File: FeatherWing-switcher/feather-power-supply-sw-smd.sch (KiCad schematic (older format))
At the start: 25 parts, among them J1 5.08mm, J2 Conn_01x12, J3 Conn_01x16, J4 QWIIC, U1 TPS5405DR

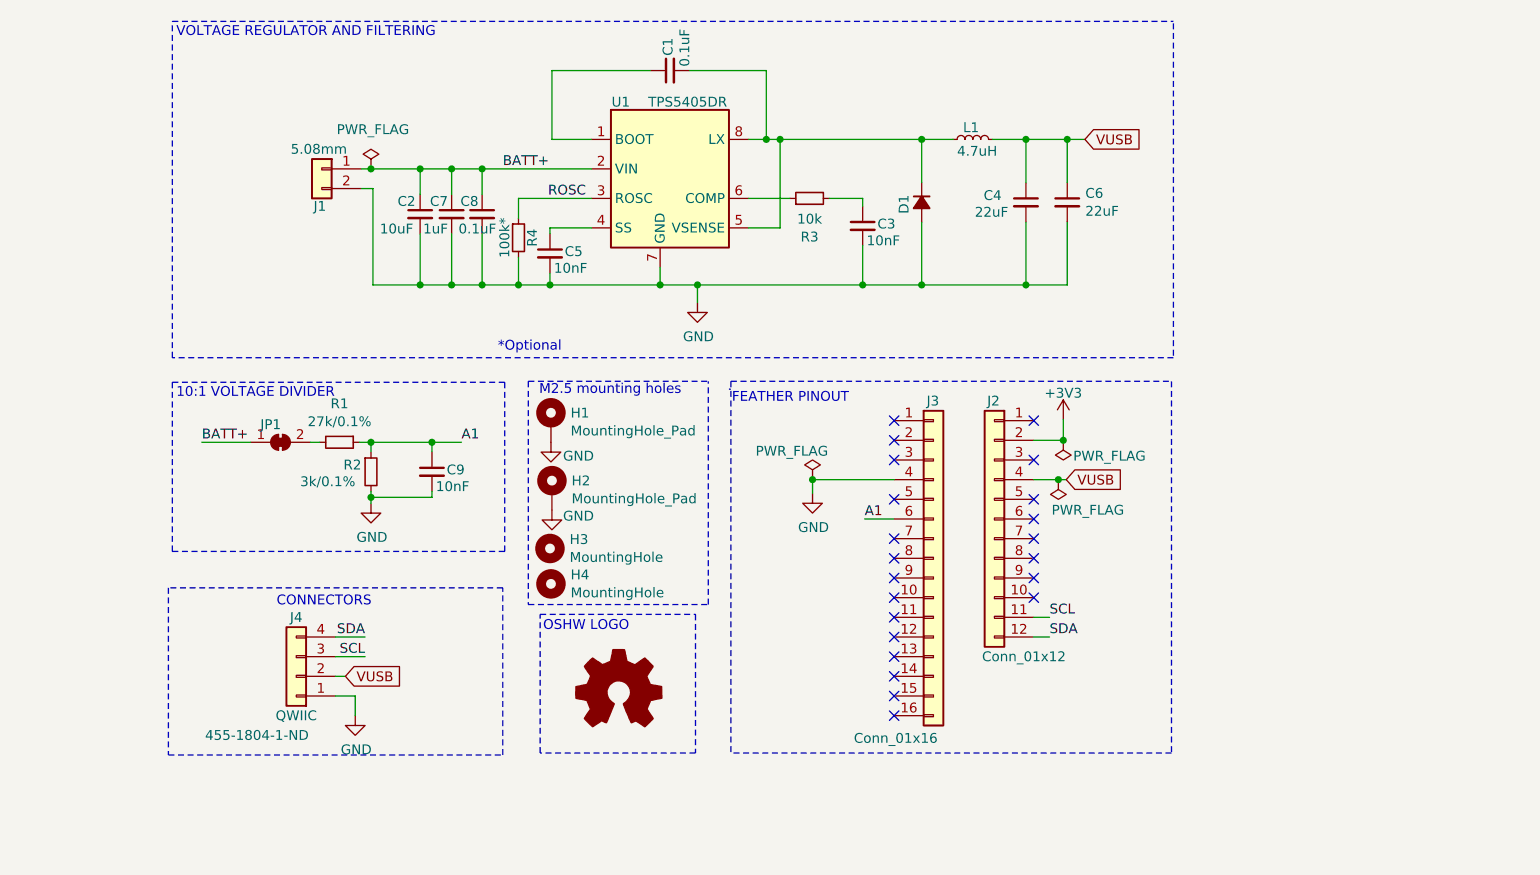
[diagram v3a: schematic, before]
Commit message: adds proto and leds
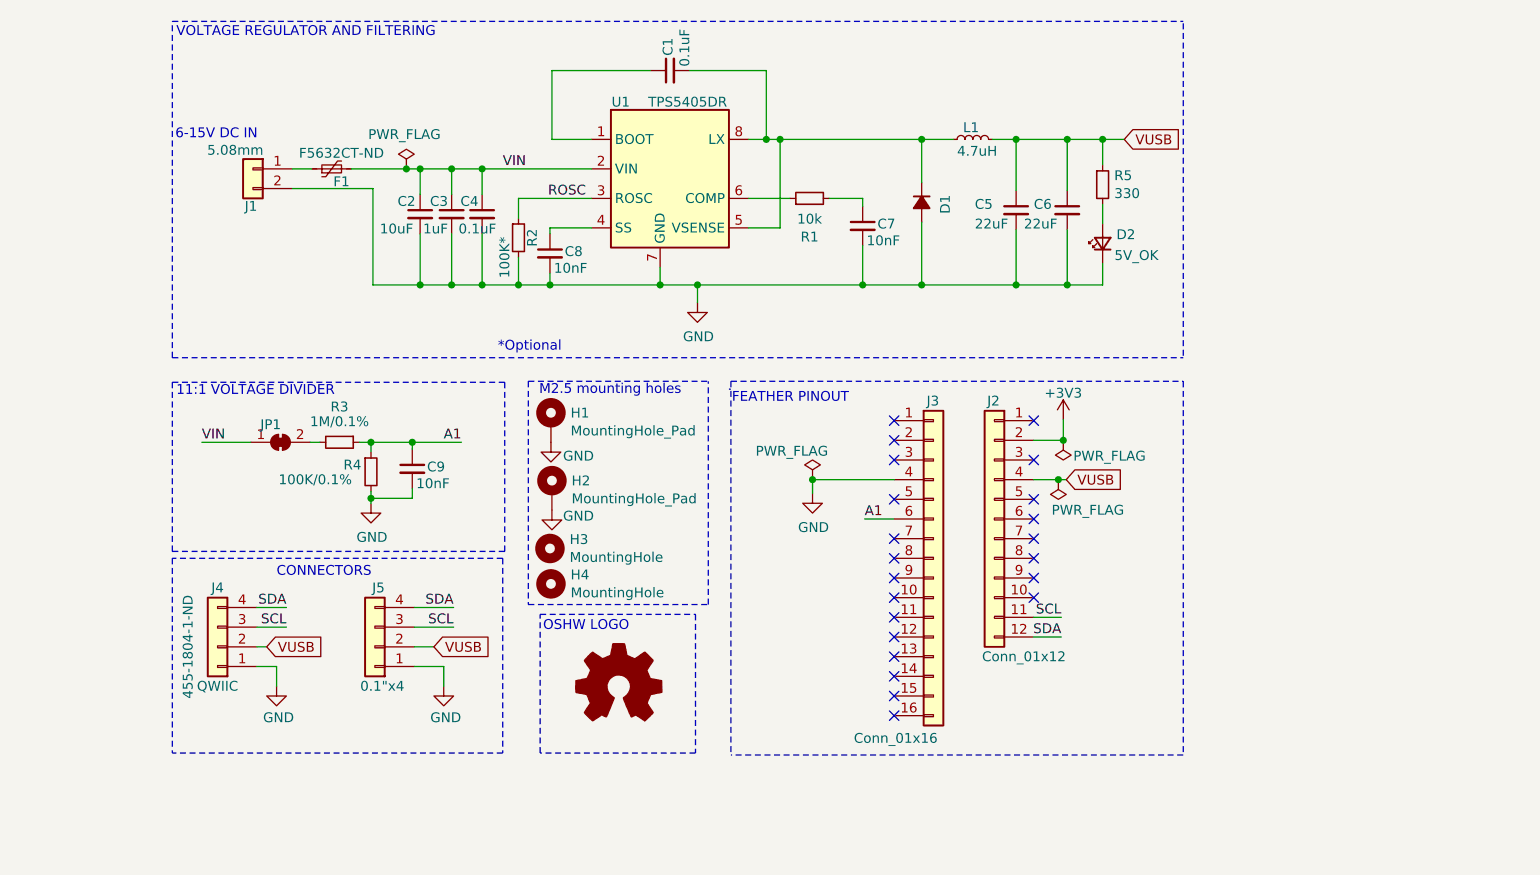
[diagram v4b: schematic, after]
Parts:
- added D2: 5V_OK, LED_SMD:LED_0805_2012Metric_Castellated, symbol Device:LED_Small
- added F1: 24V 1.1A, Fuse:Fuse_1812_4532Metric_Castellated, symbol Device:Polyfuse_Small
- added J5: 0.1\"x4, Connector_PinHeader_2.54mm:PinHeader_1x04_P2.54mm_Vertical, symbol Connector_Generic:Conn_01x04
- added LOGO1: Logo_Open_Hardware_Small, Symbol:OSHW-Symbol_6.7x6mm_SilkScreen, symbol Graphic:Logo_Open_Hardware_Small
- added R5: 330, Resistor_SMD:R_0603_1608Metric_Pad1.05x0.95mm_HandSolder, symbol Device:R_Small
- R2: renamed from R4; value 100k* -> 100K*
- R3: renamed from R1; value 27k/0.1% -> 1M/0.1%
- R4: renamed from R2; value 3k/0.1% -> 100K/0.1%
- renumbered C7 to C3, C8 to C4, C4 to C5, C3 to C7, C5 to C8, R3 to R1
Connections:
- net GND: now also D2.1 (K), J5.1 (Pin_1)
- net SCL: now also J5.3 (Pin_3)
- net SDA: now also J5.4 (Pin_4)
- net VUSB: now also J5.2 (Pin_2), R5.1
- net BATT+ renamed VIN
- net VIN: now also F1.2; no longer J1.1 (Pin_1)
- new net: F1.1, J1.1 (Pin_1)
- new net: D2.2 (A), R5.2
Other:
- note added: "11:1 VOLTAGE DIVIDER"
- note added: "6-15V DC IN"
- note removed: "10:1 VOLTAGE DIVIDER"
- moved on the sheet: C5, C6, C9, J1, J4

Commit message: major updates to route buses using  copper pours
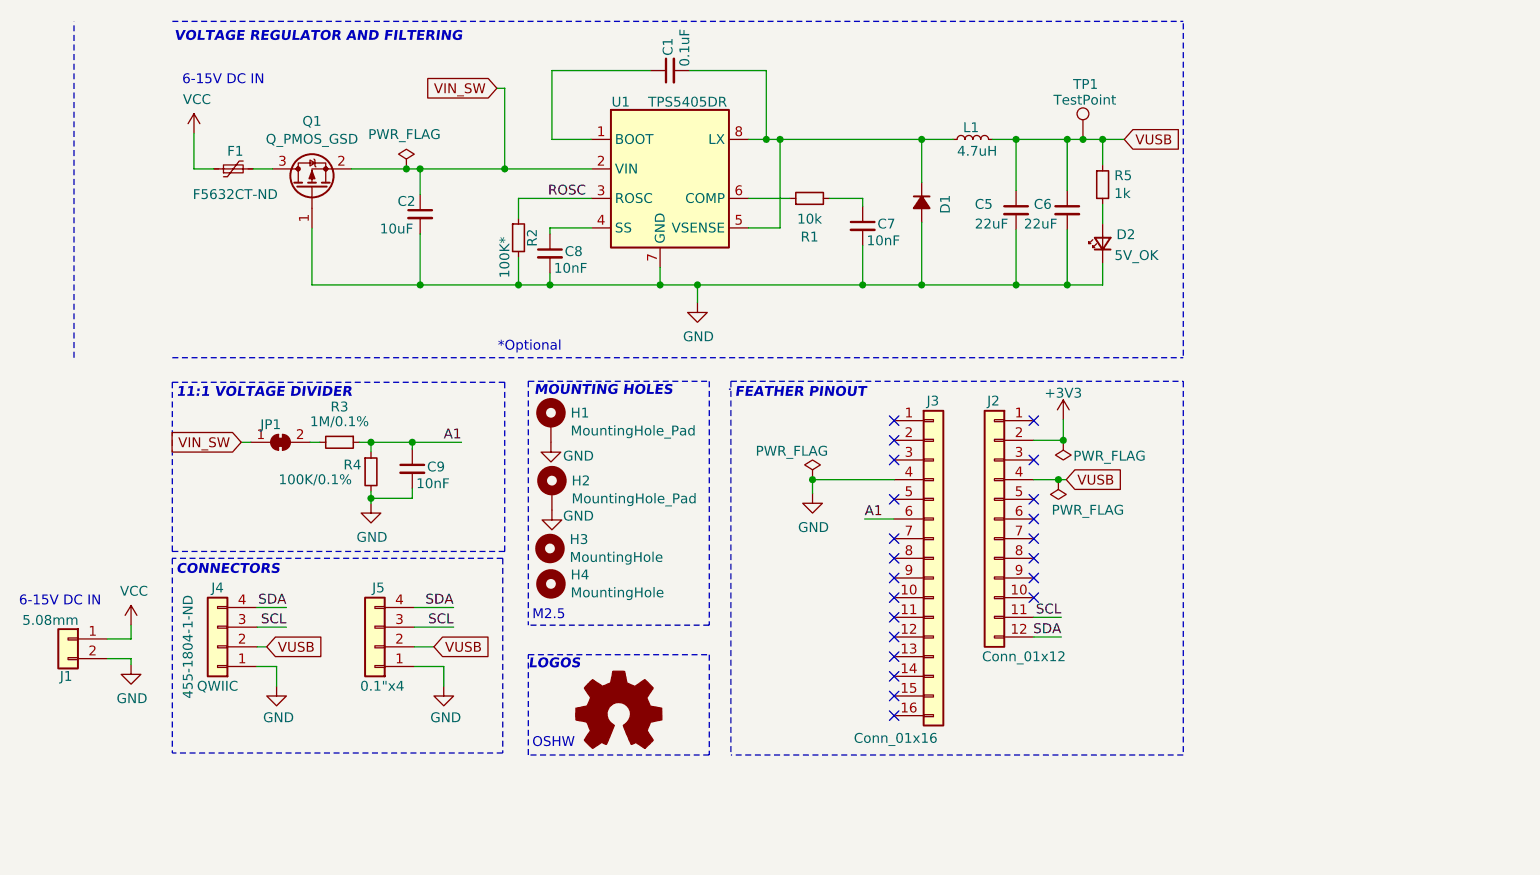
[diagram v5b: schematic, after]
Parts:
- removed C3: 1uF, Capacitor_SMD:C_0603_1608Metric_Pad1.05x0.95mm_HandSolder, symbol Device:C_Small
- removed C4: 0.1uF, Capacitor_SMD:C_0603_1608Metric_Pad1.05x0.95mm_HandSolder, symbol Device:C_Small
- added Q1: Q_PMOS_GSD, Package_TO_SOT_SMD:TSOT-23, symbol Device:Q_PMOS_GSD
- added TP1: TestPoint, TestPoint:TestPoint_Pad_D1.5mm, symbol Connector:TestPoint
- R5: value 330 -> 1k
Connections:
- net GND: now also Q1.1 (G)
- net VUSB: now also TP1.1
- net VCC: now reaches F1.1, J1.1 (Pin_1)
- net VIN renamed VIN_SW
- net VIN_SW: now also Q1.2 (S); no longer F1.2
- new net: F1.2, Q1.3 (D)
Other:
- note added: "LOGOS"
- note added: "M2.5"
- note added: "MOUNTING HOLES"
- note added: "OSHW"
- note removed: "M2.5 mounting holes"
- note removed: "OSHW LOGO"
- moved on the sheet: F1, J1
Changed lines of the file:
@@
-$EndComp
-$Comp
-L Connector_Generic:Conn_01x16 J3
-U 1 1 5F435436
-P 6940 4300
-F 0 "J3" H 6905 5100 50  0000 L CNN
-F 1 "Conn_01x16" H 6535 3385 50  0000 L CNN
-F 2 "Connector_PinHeader_2.54mm:PinHeader_1x16_P2.54mm_Vertical" H 6940 4300 50  0001 C CNN
-F 3 "~" H 6940 4300 50  0001 C CNN
-	1    6940 4300
-	1    0    0    -1
 $EndComp
 $Comp
@@
 $EndComp
 Connection ~ 6325 3900
-Text Label 3220 3710 0    50   ~ 0
-VIN
 Wire Wire Line
 	6590 4100 6740 4100
@@
 Wire Wire Line
 	6160 2620 6160 2170
-Wire Wire Line
-	3680 2420 4090 2420
-Wire Wire Line
-	4090 2420 4090 2910
-Wire Wire Line
-	4090 2910 4330 2910
 Connection ~ 4330 2910
-Text Label 4750 2320 0    50   ~ 0
-VIN
 Wire Wire Line
 	4330 2320 4330 2450
-Wire Wire Line
-	4330 2320 4490 2320
-Connection ~ 4330 2320
 Text Label 4980 2470 0    50   ~ 0
 ROSC
@@
 	8210 1580 8210 3280
 Wire Notes Line
-	3070 3280 3070 1570
+	2570 3280 2570 1570
 Connection ~ 5550 2910
 $Comp
@@
 Connection ~ 7620 2170
 Wire Wire Line
-	7620 2170 7800 2170
+	7620 2170 7700 2170
 Wire Wire Line
 	7620 2630 7620 2910
@@
 Wire Wire Line
 	7360 2910 7620 2910
-$Comp
-L Connector_Generic:Conn_01x02 J1
-U 1 1 5F4365A9
-P 3480 2320
-F 0 "J1" H 3490 2130 50  0000 C CNN
-F 1 "5.08mm" H 3570 2415 50  0000 C CNN
-F 2 "TerminalBlock_Phoenix:TerminalBlock_Phoenix_MKDS-1,5-2_1x02_P5.00mm_Horizontal" H 3480 2320 50  0001 C CNN
-F 3 "~" H 3480 2320 50  0001 C CNN
-	1    3480 2320
-	-1   0    0    -1
-$EndComp
 $Comp
 L Device:R_Small R2
@@
 Wire Wire Line
 	4830 2910 4990 2910
-Text Notes 5915 3515 0    50   ~ 0
+Text Notes 5930 3490 0    50   Italic 10
 FEATHER PINOUT
-Text Notes 3090 1655 0    50   ~ 0
+Text Notes 3080 1680 0    50   Italic 10
 VOLTAGE REGULATOR AND FILTERING
 Text Notes 4725 3255 0    50   ~ 0
@@
 	1    0    0    -1
 $EndComp
-Wire Wire Line
-	4260 2320 4330 2320
-$Comp
-L Device:C_Small C3
-U 1 1 5F53386A
-P 4490 2550
-F 0 "C3" H 4380 2615 50  0000 L CNN
-F 1 "1uF" H 4345 2475 50  0000 L CNN
-F 2 "Capacitor_SMD:C_0603_1608Metric_Pad1.05x0.95mm_HandSolder" H 4490 2550 50  0001 C CNN
-F 3 "https://www.yuden.co.jp/productdata/catalog/mlcc06_e.pdf" H 4490 2550 50  0001 C CNN
-F 4 "587-2396-1-ND" H 4490 2550 50  0001 C CNN "DigiKey_PN"
-	1    4490 2550
-	1    0    0    -1
-$EndComp
-$Comp
-L Device:C_Small C4
-U 1 1 5F533D97
-P 4645 2550
-F 0 "C4" H 4535 2615 50  0000 L CNN
-F 1 "0.1uF" H 4525 2475 50  0000 L CNN
-F 2 "Capacitor_SMD:C_0603_1608Metric_Pad1.05x0.95mm_HandSolder" H 4645 2550 50  0001 C CNN
-F 3 "https://www.yuden.co.jp/productdata/catalog/mlcc06_e.pdf" H 4645 2550 50  0001 C CNN
-F 4 "587-2396-1-ND" H 4645 2550 50  0001 C CNN "DigiKey_PN"
-	1    4645 2550
-	1    0    0    -1
-$EndComp
-Wire Wire Line
-	4490 2450 4490 2320
-Connection ~ 4490 2320
-Wire Wire Line
-	4645 2450 4645 2320
-Wire Wire Line
-	4490 2320 4645 2320
-Connection ~ 4645 2320
-Wire Wire Line
-	4645 2320 5200 2320
-Wire Wire Line
-	4645 2650 4645 2910
-Connection ~ 4645 2910
-Wire Wire Line
-	4645 2910 4830 2910
-Wire Wire Line
-	4490 2650 4490 2910
-Wire Wire Line
-	4330 2910 4490 2910
-Connection ~ 4490 2910
-Wire Wire Line
-	4490 2910 4645 2910
-Text Notes 4935 3475 0    50   ~ 0
-M2.5 mounting holes
-Wire Wire Line
-	3220 3710 3470 3710
+Text Notes 4910 3480 0    50   Italic 10
+MOUNTING HOLES
 Wire Notes Line
 	3070 4265 4760 4265
@@
 	1    0    0    -1
 $EndComp
-Text Notes 3090 3480 0    50   ~ 0
+Text Notes 3090 3490 0    50   Italic 10
 11:1 VOLTAGE DIVIDER
 Wire Wire Line
@@
 Wire Wire Line
 	4290 3710 4080 3710
-Wire Notes Line
-	5730 5290 4940 5290
-Wire Notes Line
-	4940 5290 4940 4585
-Wire Notes Line
-	4940 4585 5730 4585
-Wire Notes Line
-	5730 4585 5730 5290
-Text Notes 4955 4675 0    50   ~ 0
-OSHW LOGO
 $Comp
 L Mechanical:MountingHole H4
@@
 	1    0    0    -1
 $EndComp
-Wire Notes Line
-	4880 4535 5795 4535
-Wire Notes Line
-	5795 4535 5795 3400
-Wire Notes Line
-	4880 3400 5795 3400
-Wire Notes Line
-	4880 3400 4880 4535
 $Comp
 L Connector_Generic:Conn_01x04 J4
@@
 Wire Wire Line
 	3500 4750 3550 4750
-Text Notes 3600 4400 0    50   ~ 0
+Text Notes 3090 4390 0    50   Italic 10
 CONNECTORS
 $Comp
 L Graphic:Logo_Open_Hardware_Small LOGO1
 U 1 1 5F5741D6
-P 5340 4955
-F 0 "LOGO1" H 5340 5230 50  0001 C CNN
-F 1 "Logo_Open_Hardware_Small" H 5340 4730 50  0001 C CNN
-F 2 "Symbol:OSHW-Symbol_6.7x6mm_SilkScreen" H 5340 4955 50  0001 C CNN
-F 3 "~" H 5340 4955 50  0001 C CNN
-	1    5340 4955
-	1    0    0    -1
-$EndComp
-Text Notes 3085 2175 0    50   ~ 0
+P 5340 5095
+F 0 "LOGO1" H 5340 5370 50  0001 C CNN
+F 1 "Logo_Open_Hardware_Small" H 5340 4870 50  0001 C CNN
+F 2 "Symbol:OSHW-Symbol_6.7x6mm_SilkScreen" H 5340 5095 50  0001 C CNN
+F 3 "~" H 5340 5095 50  0001 C CNN
+	1    5340 5095
+	1    0    0    -1
+$EndComp
+Text Notes 2290 4550 0    50   ~ 0
 6-15V DC IN
 $Comp
 L Device:Polyfuse_Small F1
 U 1 1 5F5C90E5
-P 3880 2320
-F 0 "F1" V 3815 2270 50  0000 C CNN
-F 1 "24V 1.1A" V 3994 2320 50  0001 C CNN
-F 2 "Fuse:Fuse_1812_4532Metric_Castellated" H 3930 2120 50  0001 L CNN
-F 3 "~" H 3880 2320 50  0001 C CNN
-F 4 "F5632CT-ND" V 3960 2270 50  0000 C CNN "DigiKey-PN"
-F 5 "1812L110/24DR" V 3880 2320 50  0001 C CNN "MPN"
-F 6 "Littelfuse Inc." V 3880 2320 50  0001 C CNN "LittleFuse"
-	1    3880 2320
+P 3380 2320
+F 0 "F1" V 3470 2310 50  0000 C CNN
+F 1 "24V 1.1A" V 3494 2320 50  0001 C CNN
+F 2 "Fuse:Fuse_1812_4532Metric_Castellated" H 3430 2120 50  0001 L CNN
+F 3 "~" H 3380 2320 50  0001 C CNN
+F 4 "F5632CT-ND" V 3250 2310 50  0000 C CNN "DigiKey-PN"
+F 5 "1812L110/24DR" V 3380 2320 50  0001 C CNN "MPN"
+F 6 "Littelfuse Inc." V 3380 2320 50  0001 C CNN "LittleFuse"
+	1    3380 2320
 	0    -1   -1   0
 $EndComp
@@
 Connection ~ 4260 2320
 Wire Wire Line
-	3780 2320 3680 2320
+	3280 2320 3180 2320
 Wire Notes Line
 	4750 4300 3070 4300
@@
 	-1   0    0    1
 $EndComp
-Text Label 4500 4550 2    50   ~ 0
-SDA
 Text Label 4500 4650 2    50   ~ 0
 SCL
@@
 P 7800 2400
 F 0 "R5" H 7859 2446 50  0000 L CNN
-F 1 "330" H 7859 2355 50  0000 L CNN
+F 1 "1k" H 7859 2355 50  0000 L CNN
 F 2 "Resistor_SMD:R_0603_1608Metric_Pad1.05x0.95mm_HandSolder" H 7800 2400 50  0001 C CNN
 F 3 "~" H 7800 2400 50  0001 C CNN
@@
 Text Label 7590 4600 2    50   ~ 0
 SCL
+$Comp
+L Connector_Generic:Conn_01x16 J3
+U 1 1 5F435436
+P 6940 4300
+F 0 "J3" H 6905 5100 50  0000 L CNN
+F 1 "Conn_01x16" H 6535 3385 50  0000 L CNN
+F 2 "Connector_PinHeader_2.54mm:PinHeader_1x16_P2.54mm_Vertical" H 6940 4300 50  0001 C CNN
+F 3 "~" H 6940 4300 50  0001 C CNN
+	1    6940 4300
+	1    0    0    -1
+$EndComp
+Text Label 4500 4550 2    50   ~ 0
+SDA
+$Comp
+L power:VCC #PWR09
+U 1 1 5F6B3715
+P 3180 2140
+F 0 "#PWR09" H 3180 1990 50  0001 C CNN
+F 1 "VCC" H 3195 2313 50  0000 C CNN
+F 2 "" H 3180 2140 50  0001 C CNN
+F 3 "" H 3180 2140 50  0001 C CNN
+	1    3180 2140
+	1    0    0    -1
+$EndComp
+Wire Wire Line
+	3180 2140 3180 2320
+$Comp
+L Device:Q_PMOS_GSD Q1
+U 1 1 5F6B889D
+P 3780 2420
+F 0 "Q1" V 4122 2420 50  0000 C CNN
+F 1 "Q_PMOS_GSD" V 4031 2420 50  0000 C CNN
+F 2 "Package_TO_SOT_SMD:TSOT-23" H 3980 2520 50  0001 C CNN
+F 3 "~" H 3780 2420 50  0001 C CNN
+	1    3780 2420
+	0    -1   -1   0
+$EndComp
+Wire Wire Line
+	3480 2320 3580 2320
+Wire Wire Line
+	3780 2910 3780 2620
+Wire Wire Line
+	3780 2910 4330 2910
+$Comp
+L power:VCC #PWR010
+U 1 1 5F6D87E2
+P 2860 4640
+F 0 "#PWR010" H 2860 4490 50  0001 C CNN
+F 1 "VCC" H 2875 4813 50  0000 C CNN
+F 2 "" H 2860 4640 50  0001 C CNN
+F 3 "" H 2860 4640 50  0001 C CNN
+	1    2860 4640
+	1    0    0    -1
+$EndComp
+$Comp
+L power:GND #PWR011
+U 1 1 5F6D9688
+P 2860 4840
+F 0 "#PWR011" H 2860 4590 50  0001 C CNN
+F 1 "GND" H 2865 4667 50  0000 C CNN
+F 2 "" H 2860 4840 50  0001 C CNN
+F 3 "" H 2860 4840 50  0001 C CNN
+	1    2860 4840
+	1    0    0    -1
+$EndComp
+Wire Wire Line
+	2740 4710 2860 4710
+Wire Wire Line
+	2860 4710 2860 4640
+Wire Wire Line
+	2860 4840 2860 4810
+Wire Wire Line
+	2860 4810 2740 4810
+$Comp
+L Connector:TestPoint TP1
+U 1 1 5F70232D
+P 7700 2170
+F 0 "TP1" H 7650 2450 50  0000 L CNN
+F 1 "TestPoint" H 7550 2370 50  0000 L CNN
+F 2 "TestPoint:TestPoint_Pad_D1.5mm" H 7900 2170 50  0001 C CNN
+F 3 "~" H 7900 2170 50  0001 C CNN
+	1    7700 2170
+	1    0    0    -1
+$EndComp
+Connection ~ 7700 2170
+Wire Wire Line
+	7700 2170 7800 2170
+Text Notes 4900 4620 0    50   ~ 0
+M2.5
+Wire Notes Line
+	4880 3400 5800 3400
+Wire Notes Line
+	5800 4640 4880 4640
+Wire Notes Line
+	4880 3400 4880 4640
+Wire Notes Line
+	5800 3400 5800 4640
+Wire Notes Line
+	5800 4790 5800 5300
+Wire Notes Line
+	5800 5300 4880 5300
+Wire Notes Line
+	4880 5300 4880 4790
+Wire Notes Line
+	4880 4790 5800 4790
+Text Notes 4880 4870 0    50   Italic 10
+LOGOS
+Text Notes 4900 5270 0    50   ~ 0
+OSHW
+Text Notes 3120 1900 0    50   ~ 0
+6-15V DC IN
+Wire Wire Line
+	4330 2910 4830 2910
+$Comp
+L Connector_Generic:Conn_01x02 J1
+U 1 1 5F4365A9
+P 2540 4710
+F 0 "J1" H 2550 4520 50  0000 C CNN
+F 1 "5.08mm" H 2630 4805 50  0000 C CNN
+F 2 "TerminalBlock_Phoenix:TerminalBlock_Phoenix_MKDS-1,5-2_1x02_P5.00mm_Horizontal" H 2540 4710 50  0001 C CNN
+F 3 "~" H 2540 4710 50  0001 C CNN
+	1    2540 4710
+	-1   0    0    -1
+$EndComp
+Text GLabel 4720 1910 0    50   Input ~ 0
+VIN_SW
+Wire Wire Line
+	4260 2320 4330 2320
+Wire Wire Line
+	5200 2320 4760 2320
+Connection ~ 4330 2320
+Wire Wire Line
+	4760 2320 4760 1910
+Wire Wire Line
+	4760 1910 4720 1910
+Connection ~ 4760 2320
+Wire Wire Line
+	4760 2320 4330 2320
+Text GLabel 3420 3710 0    50   Input ~ 0
+VIN_SW
+Wire Wire Line
+	3470 3710 3420 3710
 $EndSCHEMATC
